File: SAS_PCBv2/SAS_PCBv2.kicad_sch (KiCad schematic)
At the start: 0 parts

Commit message: bmp280 + LogicLevelShifterPN I2C
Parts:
- added J2: Conn_02x20_Odd_Even, Connector_PinSocket_2.54mm:PinSocket_2x20_P2.54mm_Vertical, symbol Connector_Generic:Conn_02x20_Odd_Even
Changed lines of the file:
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@@
 	(generator_version "9.0")
 	(paper "A4")
+	(symbol
+		(lib_id "Connector_Generic:Conn_02x20_Odd_Even")
+		(at 171.45 104.14 0)
+		(unit 1)
+		(exclude_from_sim no)
+		(in_bom yes)
+		(on_board yes)
+		(dnp no)
+		(fields_autoplaced yes)
+		(property "Reference" "J2"
+			(at 172.72 74.93 0)
+			(effects
+				(font
+					(size 1.27 1.27)
+				)
+			)
+		)
+		(property "Value" "Conn_02x20_Odd_Even"
+			(at 172.72 77.47 0)
+			(effects
+				(font
+					(size 1.27 1.27)
+				)
+			)
+		)
+		(property "Footprint" "Connector_PinSocket_2.54mm:PinSocket_2x20_P2.54mm_Vertical"
+			(at 171.45 104.14 0)
+			(effects
+				(font
+					(size 1.27 1.27)
+				)
+				(hide yes)
+			)
+		)
+		(property "Datasheet" "https://images.theengineeringprojects.com/image/webp/2021/03/raspberry-pi-4.png.webp?ssl=1"
+			(at 171.45 104.14 0)
+			(effects
+				(font
+					(size 1.27 1.27)
+				)
+				(hide yes)
+			)
+		)
+		(property "Description" "Raspberry Pi 4B"
+			(at 171.45 104.14 0)
+			(effects
+				(font
+					(size 1.27 1.27)
+				)
+				(hide yes)
+			)
+		)
+		(pin "23"
+		)
+		(pin "5"
+		)
+		(pin "21"
+		)
+		(pin "15"
+		)
+		(pin "19"
+		)
+		(pin "16"
+		)
+		(pin "25"
+		)
+		(pin "1"
+		)
+		(pin "31"
+		)
+		(pin "39"
+		)
+		(pin "8"
+		)
+		(pin "10"
+		)
+		(pin "3"
+		)
+		(pin "7"
+		)
+		(pin "11"
+		)
+		(pin "13"
+		)
+		(pin "17"
+		)
+		(pin "9"
+		)
+		(pin "27"
+		)
+		(pin "29"
+		)
+		(pin "33"
+		)
+		(pin "35"
+		)
+		(pin "37"
+		)
+		(pin "2"
+		)
+		(pin "4"
+		)
+		(pin "6"
+		)
+		(pin "12"
+		)
+		(pin "14"
+		)
+		(pin "36"
+		)
+		(pin "32"
+		)
+		(pin "26"
+		)
+		(pin "34"
+		)
+		(pin "20"
+		)
+		(pin "28"
+		)
+		(pin "38"
+		)
+		(pin "40"
+		)
+		(pin "22"
+		)
+		(pin "24"
+		)
+		(pin "30"
+		)
+		(pin "18"
+		)
+		(instances
+			(project ""
+				(path "/9d66b581-dc57-43dc-b827-73e5c0cd12f6"
+					(reference "J2")
+					(unit 1)
+				)
+			)
+		)
+	)
 	(sheet
 		(at 15.24 31.75)

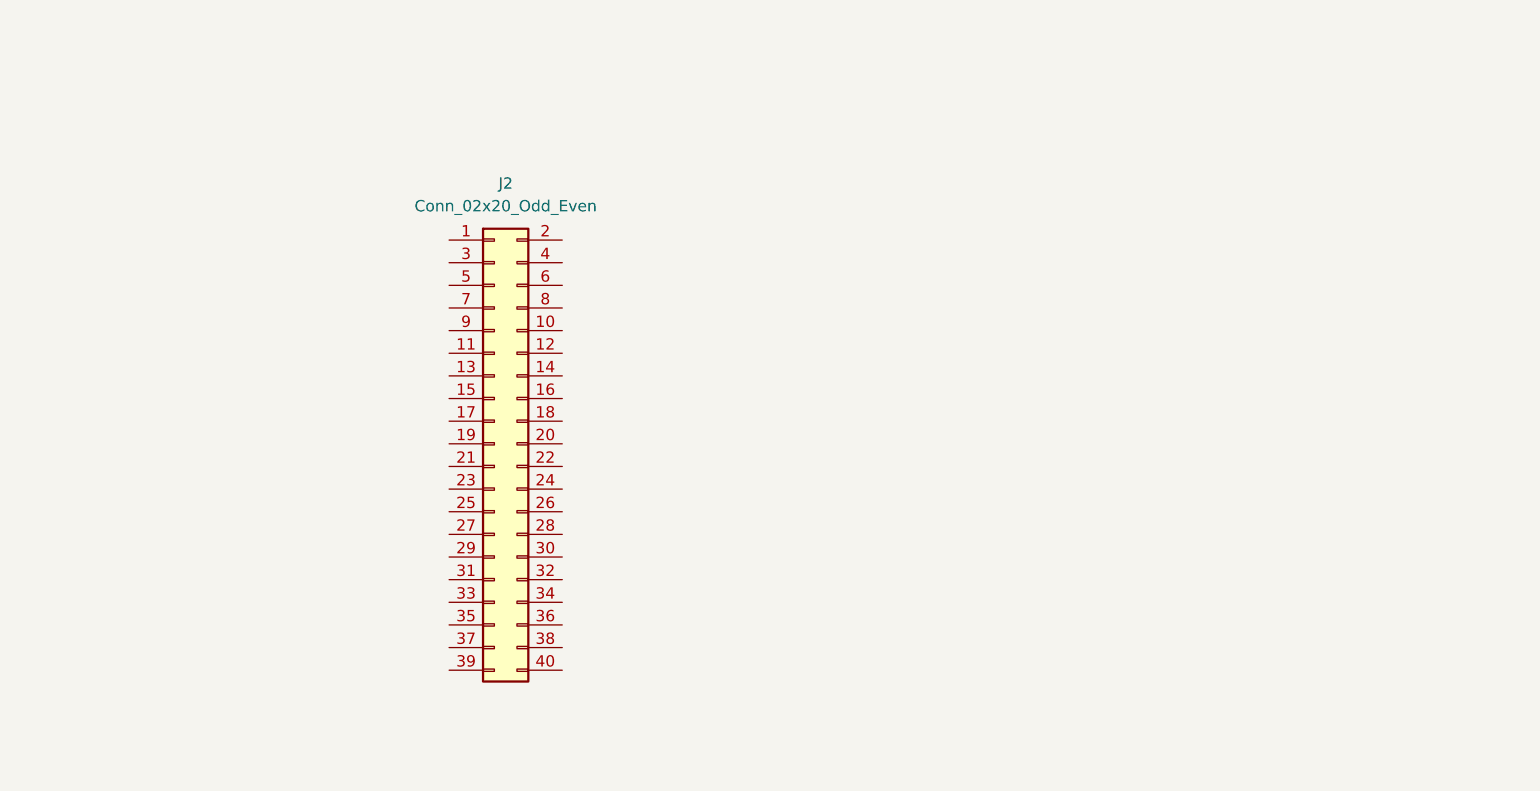
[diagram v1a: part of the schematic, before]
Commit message: Added basic Buttons w/ Rpi connections
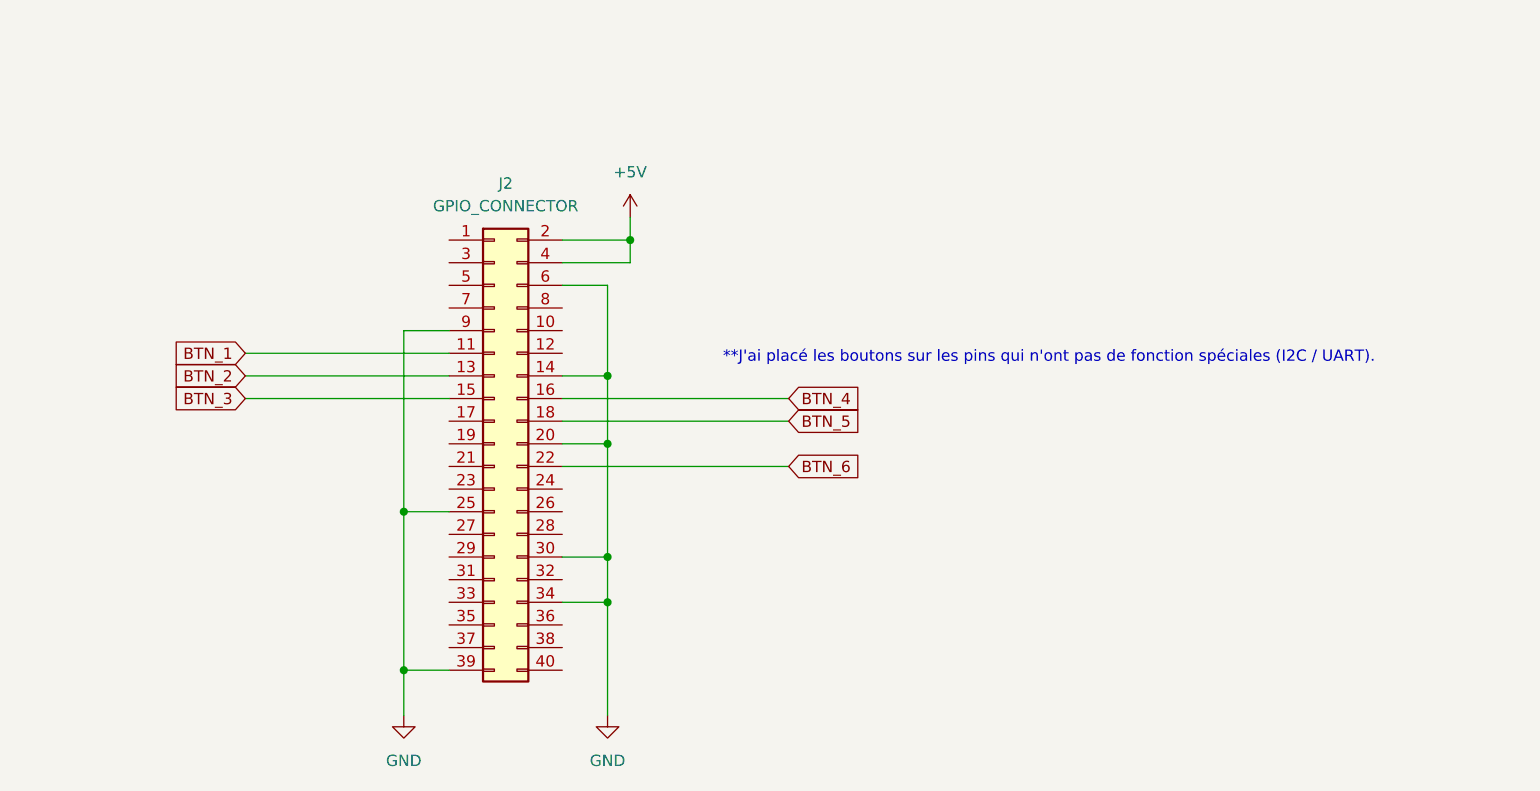
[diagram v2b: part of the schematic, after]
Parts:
- J2: value Conn_02x20_Odd_Even -> GPIO_CONNECTOR
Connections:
- net BTN_1: now reaches J2.11 (Pin_11)
- net BTN_2: now reaches J2.13 (Pin_13)
- net GND: now reaches J2.14 (Pin_14)
- net GND: now also J2.20 (Pin_20), J2.25 (Pin_25), J2.30 (Pin_30), J2.34 (Pin_34), J2.39 (Pin_39), J2.6 (Pin_6), J2.9 (Pin_9)
- net BTN_3: now reaches J2.15 (Pin_15)
- net BTN_4: now reaches J2.16 (Pin_16)
- net BTN_5: now reaches J2.18 (Pin_18)
- net +5V: now reaches J2.2 (Pin_2)
- net +5V: now also J2.4 (Pin_4)
- net BTN_6: now reaches J2.22 (Pin_22)
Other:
- note added: "**J'ai placé les boutons sur les pins qui n'ont pas de fonction spéciales (I2C / UART)."

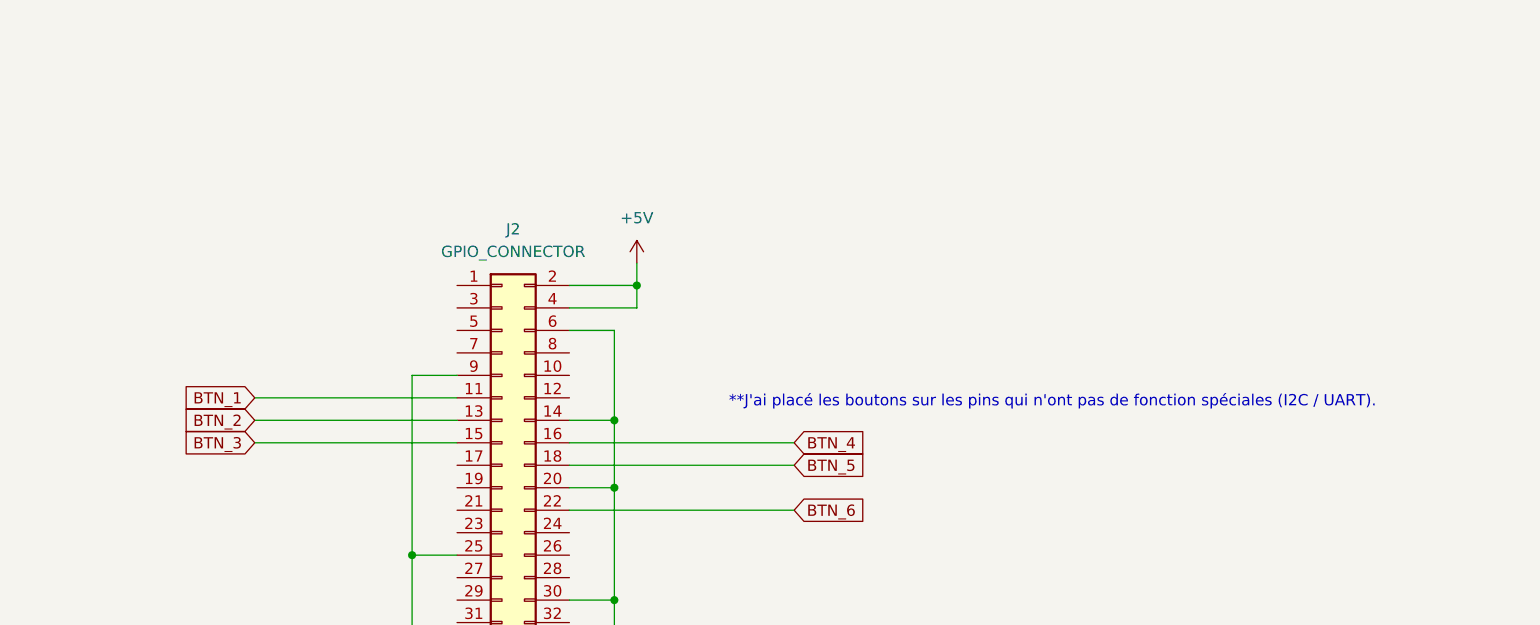
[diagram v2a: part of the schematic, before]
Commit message: Added secondary displays, completed LDO 3V3
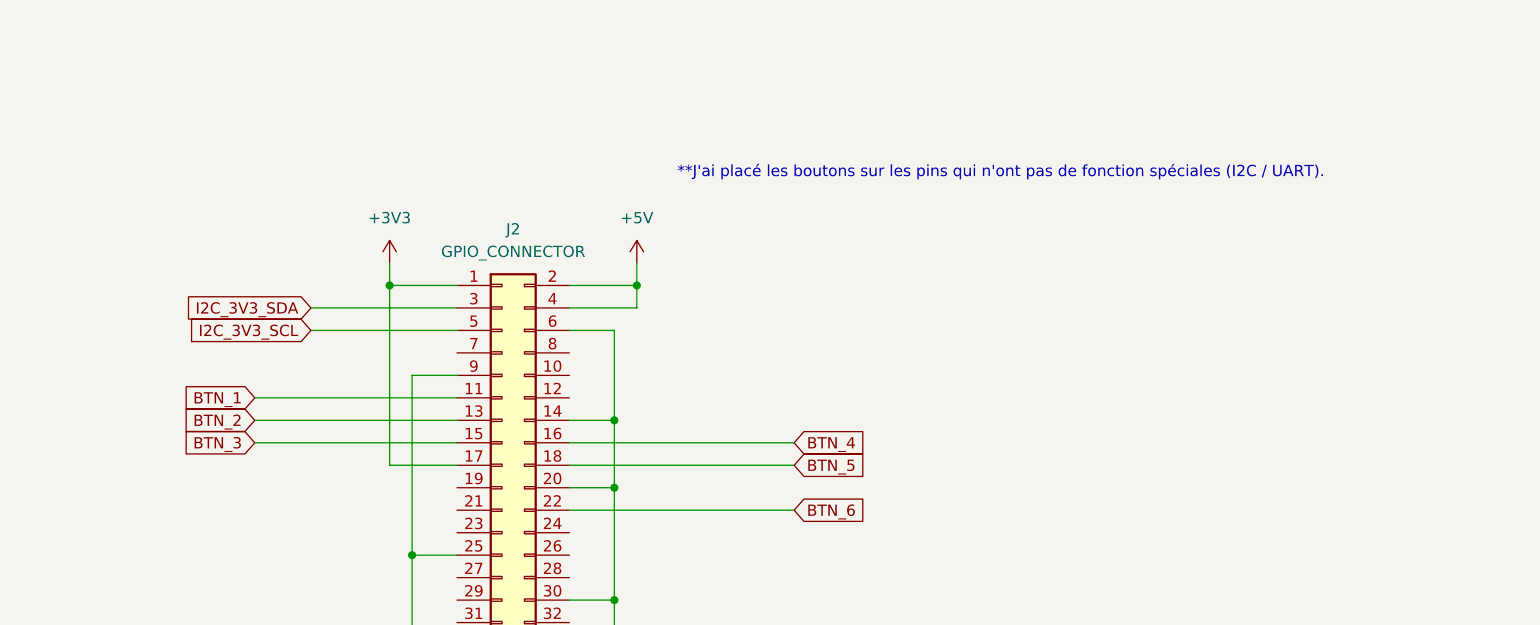
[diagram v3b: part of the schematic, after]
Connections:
- net +3V3: now reaches J2.1 (Pin_1)
- net +3V3: now also J2.17 (Pin_17)
- net I2C_3V3_SDA: now reaches J2.3 (Pin_3)
- net I2C_3V3_SCL: now reaches J2.5 (Pin_5)
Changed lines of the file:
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@@
 	(text "**J'ai placé les boutons sur les pins qui n'ont pas de fonction spéciales (I2C / UART)."
 		(exclude_from_sim no)
-		(at 233.68 94.488 0)
+		(at 227.838 68.58 0)
 		(effects
 			(font
@@
 		(color 0 0 0 0)
 	)
+	(junction
+		(at 158.75 81.28)
+		(diameter 0)
+		(color 0 0 0 0)
+	)
 	(wire
 		(pts
@@
 	(wire
 		(pts
+			(xy 158.75 81.28) (xy 166.37 81.28)
+		)
+		(stroke
+			(width 0)
+			(type default)
+		)
+	)
+	(wire
+		(pts
+			(xy 149.86 86.36) (xy 166.37 86.36)
+		)
+		(stroke
+			(width 0)
+			(type default)
+		)
+	)
+	(wire
+		(pts
+			(xy 158.75 81.28) (xy 158.75 101.6)
+		)
+		(stroke
+			(width 0)
+			(type default)
+		)
+	)
+	(wire
+		(pts
 			(xy 161.29 111.76) (xy 166.37 111.76)
 		)
@@
 	(wire
 		(pts
+			(xy 166.37 101.6) (xy 158.75 101.6)
+		)
+		(stroke
+			(width 0)
+			(type default)
+		)
+	)
+	(wire
+		(pts
+			(xy 158.75 78.74) (xy 158.75 81.28)
+		)
+		(stroke
+			(width 0)
+			(type default)
+		)
+	)
+	(wire
+		(pts
 			(xy 143.51 99.06) (xy 166.37 99.06)
 		)
@@
 	(wire
 		(pts
+			(xy 149.86 83.82) (xy 166.37 83.82)
+		)
+		(stroke
+			(width 0)
+			(type default)
+		)
+	)
+	(wire
+		(pts
 			(xy 184.15 116.84) (xy 184.15 121.92)
 		)
@@
 		)
 	)
+	(global_label "I2C_3V3_SDA"
+		(shape input)
+		(at 149.86 83.82 180)
+		(fields_autoplaced yes)
+		(effects
+			(font
+				(size 1.27 1.27)
+			)
+			(justify right)
+		)
+		(property "Intersheetrefs" "${INTERSHEET_REFS}"
+			(at 134.7796 83.82 0)
+			(effects
+				(font
+					(size 1.27 1.27)
+				)
+				(justify right)
+				(hide yes)
+			)
+		)
+	)
 	(global_label "BTN_2"
 		(shape input)
@@
 		(property "Intersheetrefs" "${INTERSHEET_REFS}"
 			(at 134.7796 96.52 0)
+			(effects
+				(font
+					(size 1.27 1.27)
+				)
+				(justify right)
+				(hide yes)
+			)
+		)
+	)
+	(global_label "I2C_3V3_SCL"
+		(shape input)
+		(at 149.86 86.36 180)
+		(fields_autoplaced yes)
+		(effects
+			(font
+				(size 1.27 1.27)
+			)
+			(justify right)
+		)
+		(property "Intersheetrefs" "${INTERSHEET_REFS}"
+			(at 134.8401 86.36 0)
 			(effects
 				(font
@@
 					(unit 1)
 				)
+			)
+		)
+	)
+	(symbol
+		(lib_id "power:+3V3")
+		(at 158.75 78.74 0)
+		(unit 1)
+		(exclude_from_sim no)
+		(in_bom yes)
+		(on_board yes)
+		(dnp no)
+		(fields_autoplaced yes)
+		(property "Reference" "#PWR032"
+			(at 158.75 82.55 0)
+			(effects
+				(font
+					(size 1.27 1.27)
+				)
+				(hide yes)
+			)
+		)
+		(property "Value" "+3V3"
+			(at 158.75 73.66 0)
+			(effects
+				(font
+					(size 1.27 1.27)
+				)
+			)
+		)
+		(property "Footprint" ""
+			(at 158.75 78.74 0)
+			(effects
+				(font
+					(size 1.27 1.27)
+				)
+				(hide yes)
+			)
+		)
+		(property "Datasheet" ""
+			(at 158.75 78.74 0)
+			(effects
+				(font
+					(size 1.27 1.27)
+				)
+				(hide yes)
+			)
+		)
+		(property "Description" "Power symbol creates a global label with name \"+3V3\""
+			(at 158.75 78.74 0)
+			(effects
+				(font
+					(size 1.27 1.27)
+				)
+				(hide yes)
+			)
+		)
+		(pin "1"
+		)
+		(instances
+			(project ""
+				(path "/9d66b581-dc57-43dc-b827-73e5c0cd12f6"
+					(reference "#PWR032")
+					(unit 1)
+				)

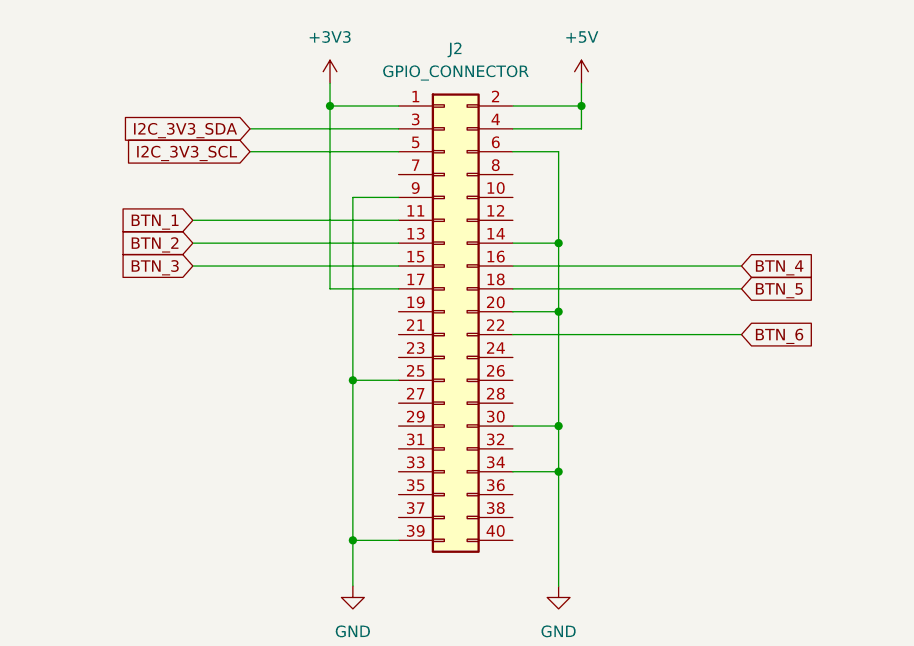
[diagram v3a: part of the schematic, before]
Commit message: Radio et GPS fait selon les datasheets normalement
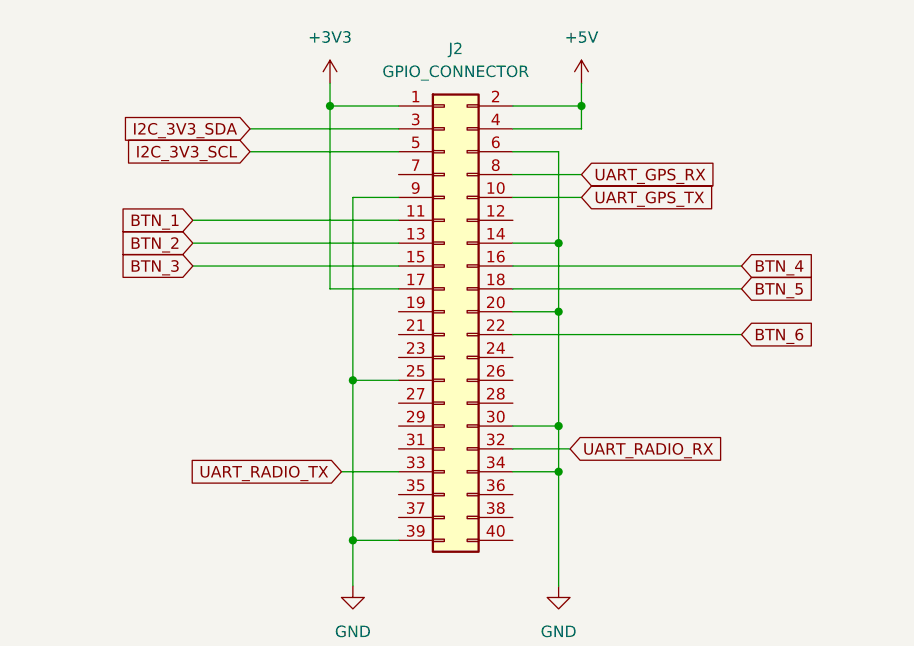
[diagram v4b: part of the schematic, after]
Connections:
- net UART_GPS_TX: now reaches J2.10 (Pin_10)
- net UART_RADIO_RX: now reaches J2.32 (Pin_32)
- net UART_RADIO_TX: now reaches J2.33 (Pin_33)
- net UART_GPS_RX: now reaches J2.8 (Pin_8)
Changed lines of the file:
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@@
+	(wire
+		(pts
+			(xy 179.07 88.9) (xy 186.69 88.9)
+		)
+		(stroke
+			(width 0)
+			(type default)
+		)
+	)
 	(wire
 		(pts
@@
 	(wire
 		(pts
+			(xy 160.02 121.92) (xy 166.37 121.92)
+		)
+		(stroke
+			(width 0)
+			(type default)
+		)
+	)
+	(wire
+		(pts
 			(xy 179.07 104.14) (xy 184.15 104.14)
 		)
@@
 	(wire
 		(pts
+			(xy 179.07 119.38) (xy 185.42 119.38)
+		)
+		(stroke
+			(width 0)
+			(type default)
+		)
+	)
+	(wire
+		(pts
 			(xy 184.15 121.92) (xy 184.15 134.62)
 		)
@@
 	(wire
 		(pts
+			(xy 179.07 91.44) (xy 186.69 91.44)
+		)
+		(stroke
+			(width 0)
+			(type default)
+		)
+	)
+	(wire
+		(pts
 			(xy 179.07 96.52) (xy 184.15 96.52)
 		)
@@
 		)
 	)
+	(global_label "UART_RADIO_RX"
+		(shape input)
+		(at 185.42 119.38 0)
+		(fields_autoplaced yes)
+		(effects
+			(font
+				(size 1.27 1.27)
+			)
+			(justify left)
+		)
+		(property "Intersheetrefs" "${INTERSHEET_REFS}"
+			(at 203.0405 119.38 0)
+			(effects
+				(font
+					(size 1.27 1.27)
+				)
+				(justify left)
+				(hide yes)
+			)
+		)
+	)
 	(global_label "BTN_3"
 		(shape input)
@@
 		)
 	)
+	(global_label "UART_RADIO_TX"
+		(shape input)
+		(at 160.02 121.92 180)
+		(fields_autoplaced yes)
+		(effects
+			(font
+				(size 1.27 1.27)
+			)
+			(justify right)
+		)
+		(property "Intersheetrefs" "${INTERSHEET_REFS}"
+			(at 142.7019 121.92 0)
+			(effects
+				(font
+					(size 1.27 1.27)
+				)
+				(justify right)
+				(hide yes)
+			)
+		)
+	)
 	(global_label "BTN_5"
 		(shape input)
@@
 				(hide yes)
 			)
+		)
+	)
+	(global_label "UART_GPS_TX"
+		(shape input)
+		(at 186.69 91.44 0)
+		(fields_autoplaced yes)
+		(effects
+			(font
+				(size 1.27 1.27)
+			)
+			(justify left)
+		)
+		(property "Intersheetrefs" "${INTERSHEET_REFS}"
+			(at 202.1937 91.44 0)
+			(effects
+				(font
+					(size 1.27 1.27)
+				)
+				(justify left)
+				(hide yes)
+			)
+		)
+	)
+	(global_label "UART_GPS_RX"
+		(shape input)
+		(at 186.69 88.9 0)
+		(fields_autoplaced yes)
+		(effects
+			(font
+				(size 1.27 1.27)
+			)
+			(justify left)
+		)
+		(property "Intersheetrefs" "${INTERSHEET_REFS}"
+			(at 202.4961 88.9 0)
+			(effects
+				(font
+					(size 1.27 1.27)
+				)
+				(justify left)
+				(hide yes)
+			)
